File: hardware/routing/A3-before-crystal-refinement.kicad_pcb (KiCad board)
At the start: 4 copper layers, 90 x 36 mm, 121 parts, among them J1 USB-C USB2.0, J2 SMA FEMALE VERTICAL 50 OHM, J3 EXPANSION (DNP), J4 POWER ARM AUTO / EXT, Q1 MMBT3904, Q2 MMBT3904, SW1 RESET, SW2 BOOT, U1 ESP32-WROOM-32E-N8, U2 CC1101RGPR, U3 PE42442A-Z, U4 PE42442A-Z, U5 CP2102N-A02-GQFN24, U6 AP63203WU-7, U7 TPS22918DBVR, U8 SN74LVC2G125DCTR, Y1 ABM8-26.000MHZ-10-1-U-T

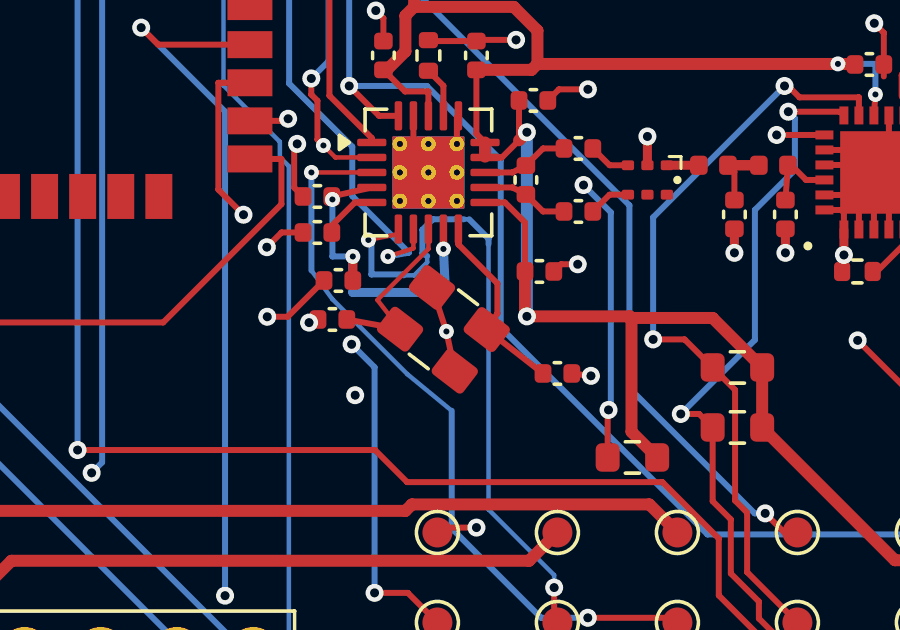
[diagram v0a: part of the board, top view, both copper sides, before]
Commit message: Refine crystal routing and add automated route margin checks
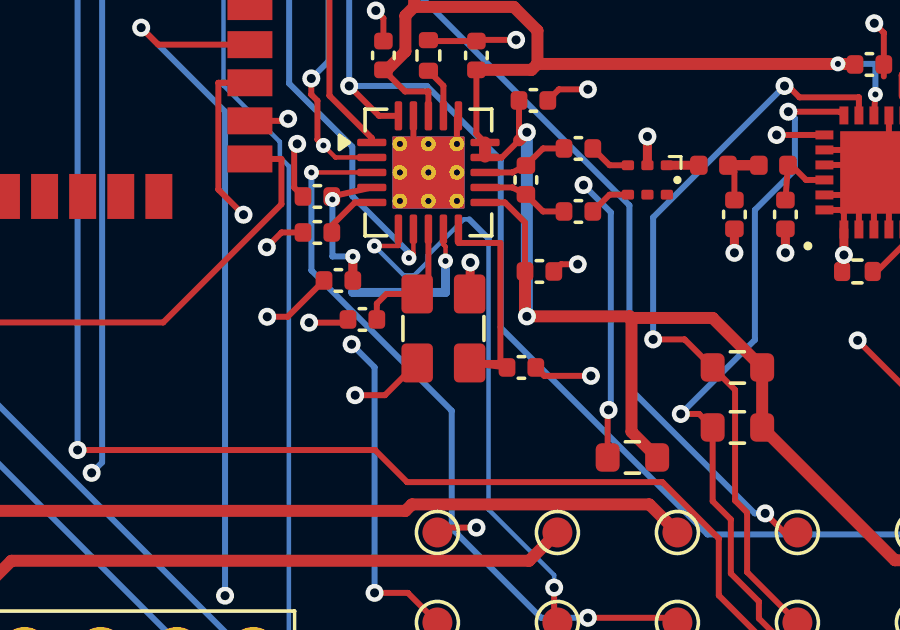
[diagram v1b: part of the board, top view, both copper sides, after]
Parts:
- moved C32 1.22 mm to (52.8, 24.5)
- moved C31 1.00 mm to (47.5, 22.9)
- turned Y1 to -90 degrees
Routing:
- net /GND: track 183.9 -> 186.9 mm
- net /CC1101_XOSC_Q2: track 6.37 -> 8.14 mm
- net /CC1101_XOSC_Q1: track 6.10 -> 4.55 mm
- net /CC1101_GDO0: track 48.0 -> 46.8 mm
- net /CC1101_CSN: track 32.8 -> 32.1 mm
